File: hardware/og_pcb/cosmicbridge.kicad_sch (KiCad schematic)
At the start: 5 parts, among them J10 Conn_02x02_Top_Bottom, J6 USB_B_Micro, J7 Conn_02x02_Top_Bottom, J8 Conn_02x02_Top_Bottom, J9 Conn_02x02_Top_Bottom

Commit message: updated pcb work in progress (incomplete)
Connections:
- net VBUS: now also J6.1 (VBUS)
- no-connect marks 1 -> 0
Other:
- note added: "connected usb to power plane as well"
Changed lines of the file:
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@@
+		)
+	)
+	(text "connected usb to power plane as well\n"
+		(exclude_from_sim no)
+		(at 100.965 71.755 0)
+		(effects
+			(font
+				(size 1.27 1.27)
+			)
 		)
 	)
@@
 		(color 0 0 0 0)
 	)
-	(no_connect
-		(at 74.93 76.2)
-	)
 	(wire
 		(pts
@@
 	(wire
 		(pts
+			(xy 78.105 76.2) (xy 78.105 74.295)
+		)
+		(stroke
+			(width 0)
+			(type default)
+		)
+	)
+	(wire
+		(pts
 			(xy 123.19 92.075) (xy 123.19 94.615)
 		)
@@
 		(pts
 			(xy 109.22 121.92) (xy 112.395 121.92)
+		)
+		(stroke
+			(width 0)
+			(type default)
+		)
+	)
+	(wire
+		(pts
+			(xy 74.93 76.2) (xy 78.105 76.2)
 		)
 		(stroke
@@
 					(unit 1)
 				)
+			)
+		)
+	)
+	(symbol
+		(lib_id "power:VBUS")
+		(at 78.105 74.295 0)
+		(unit 1)
+		(exclude_from_sim no)
+		(in_bom yes)
+		(on_board yes)
+		(dnp no)
+		(property "Reference" "#PWR04"
+			(at 78.105 78.105 0)
+			(effects
+				(font
+					(size 1.27 1.27)
+				)
+				(hide yes)
+			)
+		)
+		(property "Value" "VBUS"
+			(at 78.105 69.85 0)
+			(effects
+				(font
+					(size 1.27 1.27)
+				)
+			)
+		)
+		(property "Footprint" ""
+			(at 78.105 74.295 0)
+			(effects
+				(font
+					(size 1.27 1.27)
+				)
+				(hide yes)
+			)
+		)
+		(property "Datasheet" ""
+			(at 78.105 74.295 0)
+			(effects
+				(font
+					(size 1.27 1.27)
+				)
+				(hide yes)
+			)
+		)
+		(property "Description" "Power symbol creates a global label with name \"VBUS\""
+			(at 78.105 74.295 0)
+			(effects
+				(font
+					(size 1.27 1.27)
+				)
+				(hide yes)
+			)
+		)
+		(pin "1"
+		)
+		(instances
+			(project "og_pcb"
+				(path "/e4ef350a-b140-44e0-8bc3-973fc24bf90a/f2f75698-7215-4a2b-8285-3e4b3531a3e0"
+					(reference "#PWR04")
+					(unit 1)
+				)

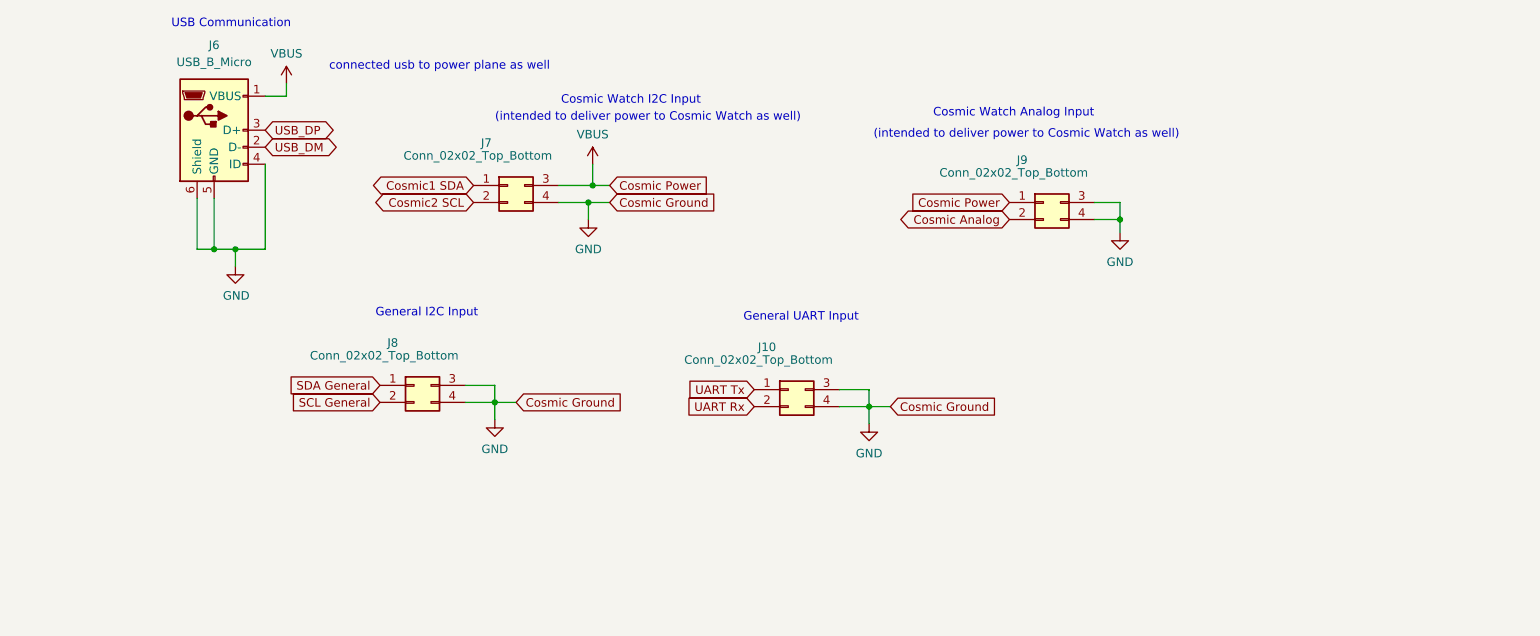
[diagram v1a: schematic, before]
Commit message: updated pcb v2 progress
reimplemented spi microSD, changed power monitor to model with internal shunt resistor, changed power supply from usbc to barrel jack, reconnected vbus to microusb, modified spi and i2c connections (2 i2c connections, 2 spi connections), removed RF module & IMU.

to do:
- find/create footprints for new parts
- verify implementation by reviewing datasheets again
- implement coax connector for analog connection to cosmic watch
- implement gps receiver (must do more research; implement one well-known/documented/used b4)
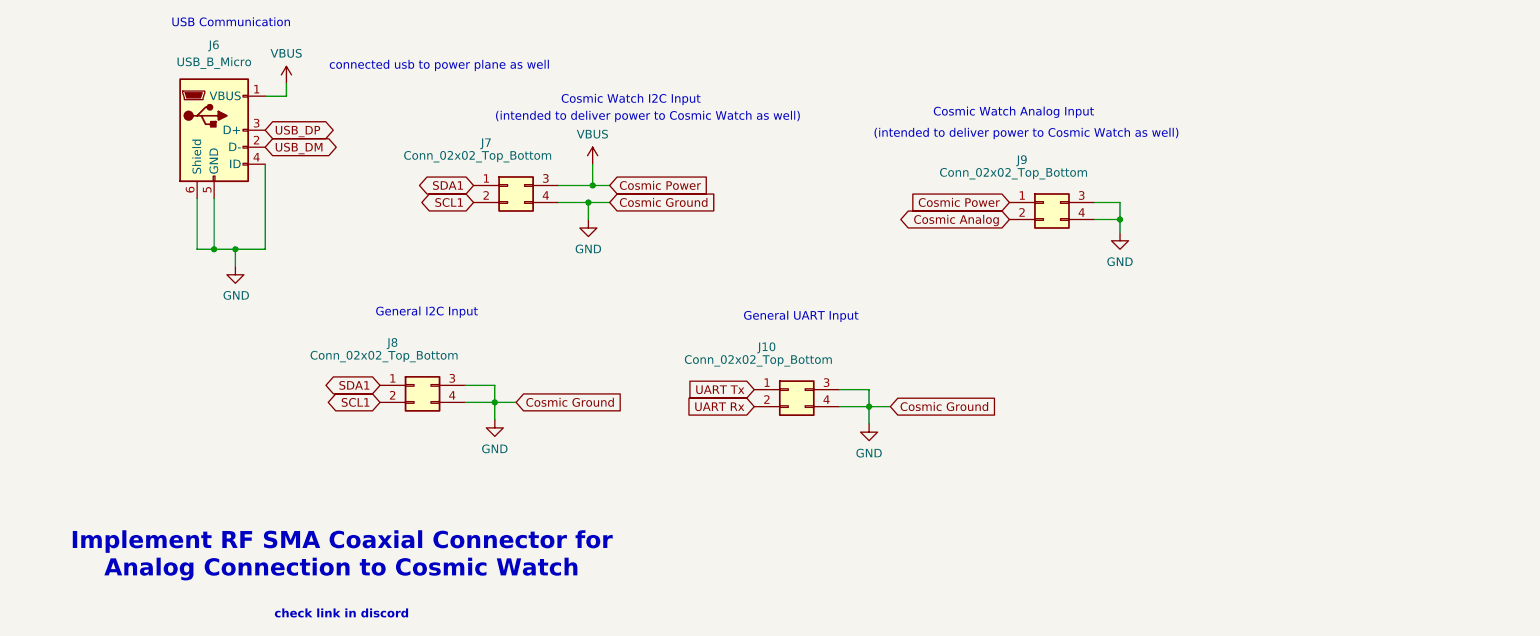
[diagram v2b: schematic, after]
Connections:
- net SCL General is gone; now on net SCL1: J8.2 (Pin_2)
- net SDA General is gone; now on net SDA1: J8.1 (Pin_1)
- net Cosmic1 SDA renamed SDA1
- net Cosmic2 SCL renamed SCL1
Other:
- note added: "Implement RF SMA Coaxial Connector for Analog Connection to Cosmic Watch"
- note added: "check link in discord"
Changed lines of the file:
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@@
+		)
+	)
+	(text "check link in discord"
+		(exclude_from_sim no)
+		(at 86.36 153.67 0)
+		(effects
+			(font
+				(size 1.27 1.27)
+				(thickness 0.254)
+				(bold yes)
+			)
 		)
 	)
@@
 			(font
 				(size 1.27 1.27)
+			)
+		)
+	)
+	(text "Implement RF SMA Coaxial Connector for \nAnalog Connection to Cosmic Watch"
+		(exclude_from_sim no)
+		(at 86.36 144.78 0)
+		(effects
+			(font
+				(size 2.54 2.54)
+				(thickness 0.254)
+				(bold yes)
 			)
 		)
@@
 		)
 	)
-	(global_label "SDA General"
-		(shape input)
-		(at 92.075 119.38 180)
-		(fields_autoplaced yes)
-		(effects
-			(font
-				(size 1.27 1.27)
-			)
-			(justify right)
-		)
-		(property "Intersheetrefs" "${INTERSHEET_REFS}"
-			(at 77.3575 119.38 0)
+	(global_label "SDA1"
+		(shape bidirectional)
+		(at 106.045 89.535 180)
+		(fields_autoplaced yes)
+		(effects
+			(font
+				(size 1.27 1.27)
+			)
+			(justify right)
+		)
+		(property "Intersheetrefs" "${INTERSHEET_REFS}"
+			(at 97.1709 89.535 0)
 			(effects
 				(font
@@
 		)
 	)
-	(global_label "Cosmic1 SDA"
-		(shape bidirectional)
-		(at 106.045 89.535 180)
-		(fields_autoplaced yes)
-		(effects
-			(font
-				(size 1.27 1.27)
-			)
-			(justify right)
-		)
-		(property "Intersheetrefs" "${INTERSHEET_REFS}"
-			(at 89.3695 89.535 0)
-			(effects
-				(font
-					(size 1.27 1.27)
-				)
-				(justify right)
-				(hide yes)
-			)
-		)
-	)
 	(global_label "USB_DM"
 		(shape bidirectional)
@@
 		)
 	)
+	(global_label "SCL1"
+		(shape bidirectional)
+		(at 106.045 92.075 180)
+		(fields_autoplaced yes)
+		(effects
+			(font
+				(size 1.27 1.27)
+			)
+			(justify right)
+		)
+		(property "Intersheetrefs" "${INTERSHEET_REFS}"
+			(at 97.2314 92.075 0)
+			(effects
+				(font
+					(size 1.27 1.27)
+				)
+				(justify right)
+				(hide yes)
+			)
+		)
+	)
+	(global_label "SDA1"
+		(shape bidirectional)
+		(at 92.075 119.38 180)
+		(fields_autoplaced yes)
+		(effects
+			(font
+				(size 1.27 1.27)
+			)
+			(justify right)
+		)
+		(property "Intersheetrefs" "${INTERSHEET_REFS}"
+			(at 83.2009 119.38 0)
+			(effects
+				(font
+					(size 1.27 1.27)
+				)
+				(justify right)
+				(hide yes)
+			)
+		)
+	)
+	(global_label "SCL1"
+		(shape bidirectional)
+		(at 92.075 121.92 180)
+		(fields_autoplaced yes)
+		(effects
+			(font
+				(size 1.27 1.27)
+			)
+			(justify right)
+		)
+		(property "Intersheetrefs" "${INTERSHEET_REFS}"
+			(at 83.2614 121.92 0)
+			(effects
+				(font
+					(size 1.27 1.27)
+				)
+				(justify right)
+				(hide yes)
+			)
+		)
+	)
 	(global_label "Cosmic Ground"
 		(shape input)
@@
 		)
 	)
-	(global_label "SCL General"
-		(shape input)
-		(at 92.075 121.92 180)
-		(fields_autoplaced yes)
-		(effects
-			(font
-				(size 1.27 1.27)
-			)
-			(justify right)
-		)
-		(property "Intersheetrefs" "${INTERSHEET_REFS}"
-			(at 77.418 121.92 0)
-			(effects
-				(font
-					(size 1.27 1.27)
-				)
-				(justify right)
-				(hide yes)
-			)
-		)
-	)
 	(global_label "Cosmic Power"
 		(shape input)
@@
 			(effects
 				(font
-					(size 1.27 1.27)
-				)
-				(justify right)
-				(hide yes)
-			)
-		)
-	)
-	(global_label "Cosmic2 SCL"
-		(shape bidirectional)
-		(at 106.045 92.075 180)
-		(fields_autoplaced yes)
-		(effects
-			(font
-				(size 1.27 1.27)
-			)
-			(justify right)
-		)
-		(property "Intersheetrefs" "${INTERSHEET_REFS}"
-			(at 89.43 92.075 0)
-			(effects
-				(font

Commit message: new preliminary demo pcb
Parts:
- added J1: Conn_Coaxial, Connector_Coaxial:MMCX_Molex_73415-1471_Vertical, symbol Connector:Conn_Coaxial
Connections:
- net Cosmic Analog: now also J1.1 (In)
- net GND: now also J1.2 (Ext)
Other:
- note added: "new cosmic watch analog input"
- note removed: "Implement RF SMA Coaxial Connector for Analog Connection to Cosmic Watch"
- note removed: "check link in discord"
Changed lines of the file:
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@@
-		)
-	)
-	(text "check link in discord"
-		(exclude_from_sim no)
-		(at 86.36 153.67 0)
-		(effects
-			(font
-				(size 1.27 1.27)
-				(thickness 0.254)
-				(bold yes)
-			)
 		)
 	)
@@
 		)
 	)
-	(text "Implement RF SMA Coaxial Connector for \nAnalog Connection to Cosmic Watch"
-		(exclude_from_sim no)
-		(at 86.36 144.78 0)
-		(effects
-			(font
-				(size 2.54 2.54)
-				(thickness 0.254)
-				(bold yes)
+	(text "new cosmic watch analog input"
+		(exclude_from_sim no)
+		(at 207.645 108.585 0)
+		(effects
+			(font
+				(size 1.27 1.27)
 			)
 		)
@@
 				)
 				(justify left)
+				(hide yes)
+			)
+		)
+	)
+	(global_label "Cosmic Analog"
+		(shape bidirectional)
+		(at 186.055 104.14 180)
+		(fields_autoplaced yes)
+		(effects
+			(font
+				(size 1.27 1.27)
+			)
+			(justify right)
+		)
+		(property "Intersheetrefs" "${INTERSHEET_REFS}"
+			(at 167.8073 104.14 0)
+			(effects
+				(font
+					(size 1.27 1.27)
+				)
+				(justify right)
 				(hide yes)
 			)
@@
 	)
 	(symbol
+		(lib_id "power:GND")
+		(at 191.135 109.22 0)
+		(unit 1)
+		(exclude_from_sim no)
+		(in_bom yes)
+		(on_board yes)
+		(dnp no)
+		(fields_autoplaced yes)
+		(property "Reference" "#PWR018"
+			(at 191.135 115.57 0)
+			(effects
+				(font
+					(size 1.27 1.27)
+				)
+				(hide yes)
+			)
+		)
+		(property "Value" "GND"
+			(at 191.135 113.665 0)
+			(effects
+				(font
+					(size 1.27 1.27)
+				)
+			)
+		)
+		(property "Footprint" ""
+			(at 191.135 109.22 0)
+			(effects
+				(font
+					(size 1.27 1.27)
+				)
+				(hide yes)
+			)
+		)
+		(property "Datasheet" ""
+			(at 191.135 109.22 0)
+			(effects
+				(font
+					(size 1.27 1.27)
+				)
+				(hide yes)
+			)
+		)
+		(property "Description" "Power symbol creates a global label with name \"GND\" , ground"
+			(at 191.135 109.22 0)
+			(effects
+				(font
+					(size 1.27 1.27)
+				)
+				(hide yes)
+			)
+		)
+		(pin "1"
+		)
+		(instances
+			(project "og_pcb"
+				(path "/e4ef350a-b140-44e0-8bc3-973fc24bf90a/f2f75698-7215-4a2b-8285-3e4b3531a3e0"
+					(reference "#PWR018")
+					(unit 1)
+				)
+			)
+		)
+	)
+	(symbol
 		(lib_id "Connector_Generic:Conn_02x02_Top_Bottom")
 		(at 191.135 92.075 0)
@@
 					(unit 1)
 				)
+			)
+		)
+	)
+	(symbol
+		(lib_id "Connector:Conn_Coaxial")
+		(at 191.135 104.14 0)
+		(unit 1)
+		(exclude_from_sim no)
+		(in_bom yes)
+		(on_board yes)
+		(dnp no)
+		(fields_autoplaced yes)
+		(property "Reference" "J1"
+			(at 194.945 103.1631 0)
+			(effects
+				(font
+					(size 1.27 1.27)
+				)
+				(justify left)
+			)
+		)
+		(property "Value" "Conn_Coaxial"
+			(at 194.945 105.7031 0)
+			(effects
+				(font
+					(size 1.27 1.27)
+				)
+				(justify left)
+			)
+		)
+		(property "Footprint" "Connector_Coaxial:MMCX_Molex_73415-1471_Vertical"
+			(at 191.135 104.14 0)
+			(effects
+				(font
+					(size 1.27 1.27)
+				)
+				(hide yes)
+			)
+		)
+		(property "Datasheet" "~"
+			(at 191.135 104.14 0)
+			(effects
+				(font
+					(size 1.27 1.27)
+				)
+				(hide yes)
+			)
+		)
+		(property "Description" "coaxial connector (BNC, SMA, SMB, SMC, Cinch/RCA, LEMO, ...)"
+			(at 191.135 104.14 0)
+			(effects
+				(font
+					(size 1.27 1.27)
+				)
+				(hide yes)
+			)
+		)
+		(pin "1"
+		)
+		(pin "2"
+		)
+		(instances
+			(project ""
+				(path "/e4ef350a-b140-44e0-8bc3-973fc24bf90a/f2f75698-7215-4a2b-8285-3e4b3531a3e0"
+					(reference "J1")
+					(unit 1)
+				)

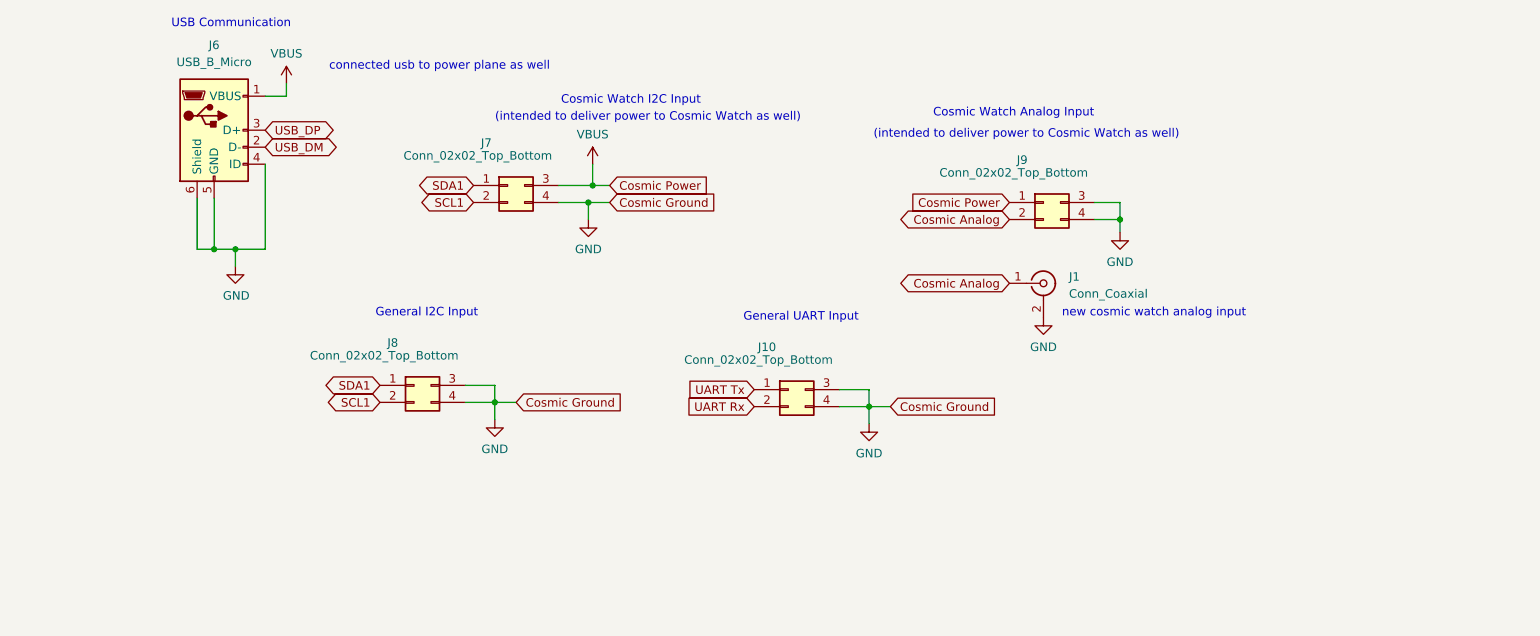
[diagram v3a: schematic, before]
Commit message: updated pcb
added footprints, led, testpoints
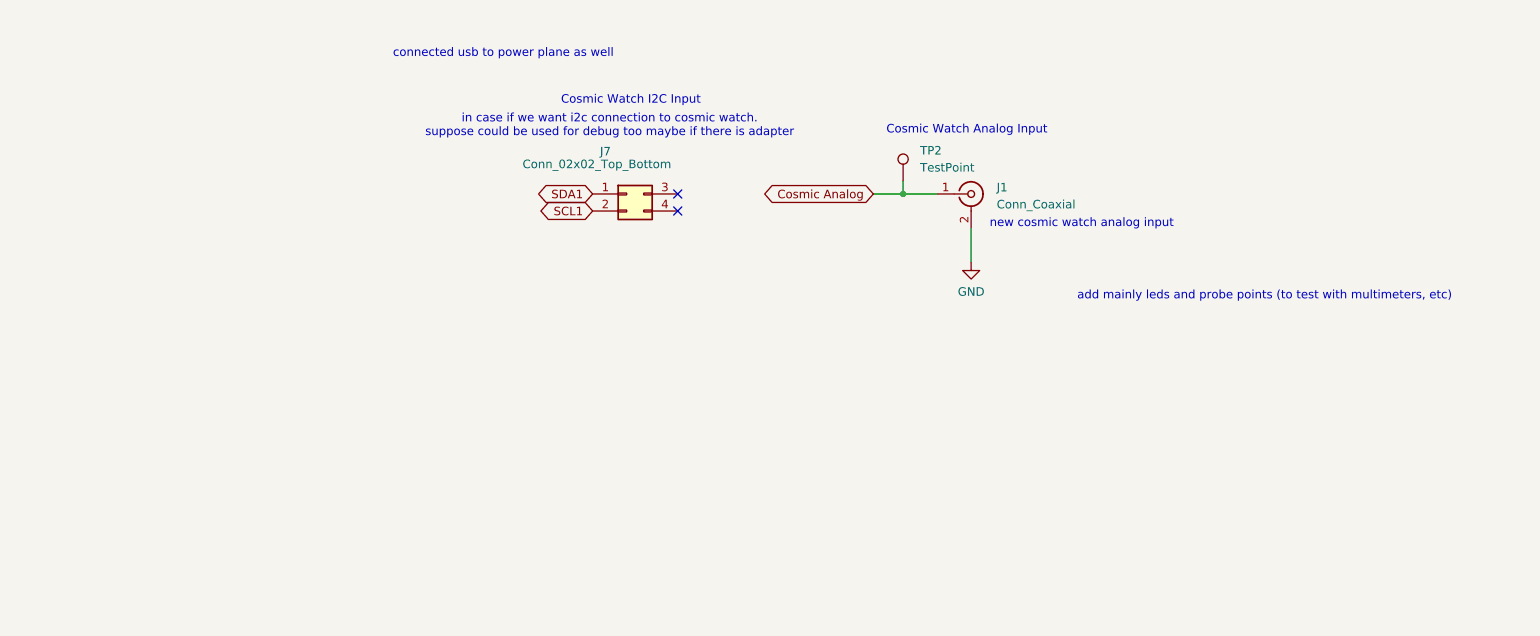
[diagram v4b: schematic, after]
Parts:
- removed J10, J8, J9: Conn_02x02_Top_Bottom, 1my_footprints:CON4_2X2_UF_DF11_HIR, symbol Connector_Generic:Conn_02x02_Top_Bottom
- removed J6: USB_B_Micro, 1my_footprints:microUSB, symbol Connector:USB_B_Micro
- added TP2: TestPoint, 1my_footprints:TestPoint_Loop_D1.80mm_Drill1.0mm_Beaded, symbol Connector:TestPoint
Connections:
- net Cosmic Analog: now also TP2.1
- net GND: no longer J7.4 (Pin_4)
- net VBUS: no longer names the net of J7.3 (Pin_3)
- no-connect marks 0 -> 2
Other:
- note added: "add mainly leds and probe points (to test with multimeters, etc)"
- note added: "in case if we want i2c connection to cosmic watch. suppose could be used for debug too maybe if there is adapter"
- note removed: "(intended to deliver power to Cosmic Watch as well)"
- note removed: "General I2C Input"
- note removed: "General UART Input"
- note removed: "USB Communication"
- moved on the sheet: J1, J7

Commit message: added comments from pragun's review
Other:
- note added: "add coax cable or another connection that will send 5V supply to cosmic watch pcb"
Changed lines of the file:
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@@
+		)
+	)
+	(text "add coax cable or another connection that will send 5V supply to\ncosmic watch pcb"
+		(exclude_from_sim no)
+		(at 147.32 118.745 0)
+		(effects
+			(font
+				(size 1.27 1.27)
+				(thickness 0.254)
+				(bold yes)
+			)
 		)
 	)
